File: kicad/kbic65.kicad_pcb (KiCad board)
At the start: 2 copper layers, 313.3 x 131.6 mm, 154 parts, among them U1 ProMicro

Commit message: pre-updating gnd
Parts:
- added ?: , , B.Cu at (-0.79, 166.7)
- added ?: , , B.Cu at (56.4, 83.3)
- R Shift: renamed from RShift
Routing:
- net Net-(D_Equal1-Pad2): track 35.2 -> 31.6 mm
- net Net-(D_@1-Pad2): track 79.2 -> 76.4 mm
- net Net-(D_LBKT1-Pad2): track 53.1 -> 50.6 mm
- net Net-(D_BKSLSH1-Pad2): track 93.8 -> 94.4 mm
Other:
- board text added: "#"
- board text added: "'"
- board text added: ","
- board text added: "-"
- board text added: "."
- board text added: "/"
- board text added: "0"
- board text added: "1"
- board text added: "1.25u"
- board text added: "1u"
- board text added: "2"
- board text added: "2.25u"
- board text added: "2u"
- board text added: "3"
- board text added: "4"
- board text added: "5"
- board text added: "6"
- board text added: "6.25u"
- board text added: "6u"
- board text added: "7"
- board text added: "8"
- board text added: "9"
- board text added: ";"
- board text added: "="
- board text added: "A"
- board text added: "B"
- board text added: "Backspace"
- board text added: "Backspace 2"
- board text added: "C"
- board text added: "Caps Lock"
- board text added: "D"
- board text added: "Delete"
- board text added: "Down"
- board text added: "E"
- board text added: "Enter"
- board text added: "Enter ANSI"
- board text added: "Esc"
- board text added: "F"
- board text added: "G"
- board text added: "H"
- board text added: "I"
- board text added: "J"
- board text added: "K"
- board text added: "L"
- board text added: "L Alt"
- board text added: "L Ctrl"
- board text added: "L Shift"
- board text added: "L Win"
- board text added: "Left"
- board text added: "M"
- board text added: "N"
- board text added: "O"
- board text added: "P"
- board text added: "Page Down"
- board text added: "Page Up"
- board text added: "Q"
- board text added: "R"
- board text added: "R Alt"
- board text added: "R Ctrl"
- board text added: "R Shift"
- board text added: "R Win"
- board text added: "Regular"
- board text added: "Right"
- board text added: "S"
- board text added: "Space"
- board text added: "Stepped"
- board text added: "T"
- board text added: "Tab"
- board text added: "U"
- board text added: "Up"
- board text added: "V"
- board text added: "W"
- board text added: "X"
- board text added: "Y"
- board text added: "Z"
- board text added: "["
- board text added: "\"
- board text added: "\ ANSI"
- board text added: "]"
- board text added: "¬"

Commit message: adding copper fill
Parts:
- MX_BkSlsh1: renamed from \ ANSI
- MX_BkSp2: renamed from Backpace 2
- MX_BkSp3_2u1: renamed from BkSp 3
- MX_CpsLck1: renamed from Caps Lock
- MX_Enter1: renamed from Enter ANSI
- MX_LAlt1: renamed from L Alt
- MX_LCtrl1: renamed from L Ctrl
- MX_LShift_ISO1: renamed from L Shift
- MX_LWin1: renamed from L Win
- MX_PgDn1: renamed from Page Down
- MX_PgUp1: renamed from Page Up
- MX_RAlt3_1.25u_6.25u_space1: renamed from R Alt
- MX_RCtrl1: renamed from R Ctrl
- MX_RShift1: renamed from R Shift
- MX_RWin1: renamed from R Win
- renumbered 0 to D_0, 1 to D_1, 2 to D_2, 3 to D_3, 4 to D_4, 5 to D_5, 6 to D_6, 7 to D_7, 8 to D_8, 9 to D_9, ' to D_@1, A to D_A1, B to D_B1, \ to D_BKSLSH1, BkSp to D_BkSp1, BkSp2 to D_BkSp2, C to D_C1, , to D_Comma1, CpsLck to D_CpsLck1, D to D_D1, Del to D_Del1, . to D_Dot1, Down to D_Down1, E to D_E1, # to D_Enter1, = to D_Equal1, Esc to D_Esc1, F to D_F1, / to D_FwdSlsh1, G to D_G1, H to D_H1, - to D_Hyphen1, I to D_I1, \ to D_ISO_BKSLSH1, J to D_J1, K to D_K1, L to D_L1, LAlt to D_LAlt1, [ to D_LBKT1, LCtrl to D_LCtrl1, LShift to D_LShift1, LWin to D_LWin1, Left to D_Left1, M to D_M1, N to D_N1, O to D_O1, P to D_P1, PgDn to D_PgDn1, PgUp to D_PgUp1, Q to D_Q1, R to D_R1, RAlt to D_RAlt1, ] to D_RBKT1, RCtrl to D_RCtrl1, RShift to D_RShift1, RWin to D_RWin1, Right to D_Right1, S to D_S1, ; to D_SemiCol1, Space to D_Space1, T to D_T1, Tab to D_Tab1, ¬ to D_Tilde1, U to D_U1, Up to D_Up1, V to D_V1, W to D_W1, X to D_X1, Y to D_Y1, Z to D_Z1, 0 to MX_0, 1 to MX_1, 2 to MX_2, 3 to MX_3, 4 to MX_4, 5 to MX_5, 6 to MX_6, 7 to MX_7, 8 to MX_8, 9 to MX_9, ' to MX_@1, A to MX_A1, B to MX_B1, Enter to MX_BkSlash2_ISO_Enter1, Backspace to MX_BkSp1, C to MX_C1, , to MX_Comma1, D to MX_D1, Delete to MX_Del1, . to MX_Dot1, Down to MX_Down1, E to MX_E1, # to MX_Enter2_ISO_Hash1, = to MX_Equal1, Esc to MX_Esc1, F to MX_F1, / to MX_FwdSlsh1, G to MX_G1, H to MX_H1, - to MX_Hyphen1, I to MX_I1, \ to MX_ISO_BKSLSH1, J to MX_J1, K to MX_K1, L to MX_L1, [ to MX_LBKT1, Left to MX_Left1, M to MX_M1, N to MX_N1, O to MX_O1, P to MX_P1, Q to MX_Q1, R to MX_R1, ] to MX_RBKT1, Right to MX_Right1, S to MX_S1, ; to MX_SemiCol1, Space to MX_Space1_6.25u1, T to MX_T1, Tab to MX_Tab1, ¬ to MX_Tilde1, U to MX_U1, Up to MX_Up1, V to MX_V1, W to MX_W1, X to MX_X1, Y to MX_Y1, Z to MX_Z1
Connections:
- U1 pad 23: Net-(U1-Pad23) -> GND
- U1 pad 3: Net-(U1-Pad3) -> GND
- U1 pad 4: Net-(U1-Pad4) -> GND
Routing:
- net Net-(D_ISO_BKSLSH1-Pad2): track 104.4 -> 105.8 mm
- net COL2: track 106.6 -> 107.3 mm
- added copper zone on B.Cu, net GND
- added copper zone on F.Cu, net GND

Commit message: readded missing silkscreen text
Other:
- board text added: "BkSp1"
- board text added: "BkSp2"
- board text added: "CpsLck"
- board text added: "Del"
- board text added: "LAlt"
- board text added: "LCtrl"
- board text added: "LShift"
- board text added: "LWin"
- board text added: "PgDn"
- board text added: "PgUp"
- board text added: "RAlt"
- board text added: "RCtrl"
- board text added: "RShift"
- board text added: "RWin"

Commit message: added signature
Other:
- board text added: "by KarlB"
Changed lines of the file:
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@@
   (general
     (thickness 1.6)
-    (drawings 1227)
+    (drawings 1229)
     (tracks 968)
     (zones 0)
@@
   (page A3)
   (layers
-    (0 F.Cu signal hide)
-    (31 B.Cu signal hide)
+    (0 F.Cu signal)
+    (31 B.Cu signal)
     (32 B.Adhes user)
     (33 F.Adhes user)
     (34 B.Paste user)
     (35 F.Paste user)
-    (36 B.SilkS user)
+    (36 B.SilkS user hide)
     (37 F.SilkS user)
     (38 B.Mask user)
@@
     )
   )
+  (gr_text "by KarlB" (at 59.5 50) (layer B.SilkS)
+    (effects (font (size 2 2) (thickness 0.2) italic) (justify mirror))
+  )
+  (gr_text "by KarlB" (at 64.75 53.75) (layer F.SilkS)
+    (effects (font (size 2 2) (thickness 0.2) italic))
+  )
   (gr_text 1 (at 87.75 56.128095) (layer B.SilkS)

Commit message: added styled lines to top
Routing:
- net GND: track 0.00 -> 1478.9 mm, vias 0 -> 1

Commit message: added ref placeholders and created gerbers
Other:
- board text added: "JLCJLCJLCJLC"
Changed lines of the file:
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@@
   (general
     (thickness 1.6)
-    (drawings 1235)
+    (drawings 1237)
     (tracks 988)
     (zones 0)
@@
   (page A3)
   (layers
-    (0 F.Cu signal)
-    (31 B.Cu signal)
+    (0 F.Cu signal hide)
+    (31 B.Cu signal hide)
     (32 B.Adhes user)
     (33 F.Adhes user)
@@
     (visible_elements 7FFDFFFF)
     (pcbplotparams
-      (layerselection 0x010fc_ffffffff)
+      (layerselection 0x013f0_ffffffff)
       (usegerberextensions false)
       (usegerberattributes true)
@@
       (outputformat 1)
       (mirror false)
-      (drillshape 1)
+      (drillshape 0)
       (scaleselection 1)
-      (outputdirectory ""))
+      (outputdirectory "gerber"))
   )
   (net 0 "")
@@
     )
   )
+  (gr_poly (pts (xy 328.824999 44.55) (xy 327.504999 44.7) (xy 326.344999 44.92) (xy 325.244999 45.3) (xy 324.794999 45.45) (xy 325.024999 47.38) (xy 326.614999 47.24) (xy 326.654999 46.36) (xy 327.004999 45.88) (xy 327.144999 45.73) (xy 327.614999 45.56) (xy 328.014999 45.44) (xy 329.424999 45.29) (xy 331.464999 45.21) (xy 332.674999 45.19) (xy 335.514999 45.39) (xy 337.184999 45.59) (xy 337.664999 45.7) (xy 338.154999 45.91) (xy 338.514999 46.16) (xy 338.804999 46.42) (xy 338.954999 46.71) (xy 339.064999 47.04) (xy 339.124999 47.5) (xy 339.174999 47.83) (xy 339.794999 47.81) (xy 339.844999 47.05) (xy 339.784999 46.5) (xy 339.384999 45.85) (xy 338.734999 45.43) (xy 338.174999 45.17) (xy 337.144999 44.92) (xy 334.714999 44.58) (xy 333.094999 44.54) (xy 330.304999 44.49)) (layer F.SilkS) (width 0.1))
+  (gr_text JLCJLCJLCJLC (at 73.025 98.425 90) (layer F.SilkS)
+    (effects (font (size 1 1) (thickness 0.15)))
+  )
   (gr_line (start 319 56.75) (end 86.5 56.75) (layer F.Mask) (width 0.25))
   (gr_line (start 319 55.75) (end 86.5 55.75) (layer F.Mask) (width 0.25))
@@
     (effects (font (size 1 1) (thickness 0.15)))
   )
-  (gr_poly (pts (xy 353.8 44.55) (xy 355.12 44.7) (xy 356.28 44.92) (xy 357.38 45.3) (xy 357.83 45.45) (xy 357.6 47.38) (xy 356.01 47.24) (xy 355.97 46.36) (xy 355.62 45.88) (xy 355.48 45.73) (xy 355.01 45.56) (xy 354.61 45.44) (xy 353.2 45.29) (xy 351.16 45.21) (xy 349.95 45.19) (xy 347.11 45.39) (xy 345.44 45.59) (xy 344.96 45.7) (xy 344.47 45.91) (xy 344.11 46.16) (xy 343.82 46.42) (xy 343.67 46.71) (xy 343.56 47.04) (xy 343.5 47.5) (xy 343.45 47.83) (xy 342.83 47.81) (xy 342.78 47.05) (xy 342.84 46.5) (xy 343.24 45.85) (xy 343.89 45.43) (xy 344.45 45.17) (xy 345.48 44.92) (xy 347.91 44.58) (xy 349.53 44.54) (xy 352.32 44.49)) (layer F.SilkS) (width 0.1))
+  (gr_poly (pts (xy 353.8 44.55) (xy 355.12 44.7) (xy 356.28 44.92) (xy 357.38 45.3) (xy 357.812961 45.475356) (xy 357.593378 47.440046) (xy 356.019031 47.225625) (xy 355.97 46.36) (xy 355.62 45.88) (xy 355.48 45.73) (xy 355.01 45.56) (xy 354.61 45.44) (xy 353.2 45.29) (xy 351.16 45.21) (xy 349.95 45.19) (xy 347.11 45.39) (xy 345.44 45.59) (xy 344.96 45.7) (xy 344.47 45.91) (xy 344.11 46.16) (xy 343.82 46.42) (xy 343.67 46.71) (xy 343.56 47.04) (xy 343.5 47.5) (xy 343.443634 47.844032) (xy 342.857268 47.823973) (xy 342.78 47.05) (xy 342.84 46.5) (xy 343.24 45.85) (xy 343.89 45.43) (xy 344.45 45.17) (xy 345.48 44.92) (xy 347.91 44.58) (xy 349.53 44.54) (xy 352.32 44.49)) (layer F.SilkS) (width 0.1))
   (gr_line (start 49.085386 165.775001) (end 49.085386 165.775001) (layer Edge.Cuts) (width 0.2))
   (gr_line (start 46.585405 163.275001) (end 46.585399 42.30625) (layer Edge.Cuts) (width 0.2))
@@
   (gr_line (start 62.562499 72.374992) (end 62.562499 86.375408) (layer Dwgs.User) (width 0.2))
   (gr_line (start 48.562083 72.374992) (end 62.562499 72.374992) (layer Dwgs.User) (width 0.2))
-  (via (at 320 50) (size 0.8) (drill 0.4) (layers F.Cu B.Cu) (net 92))
-  (segment (start 86.5 43.25) (end 319 43.25) (width 0.3) (layer F.Cu) (net 92))
-  (segment (start 86.5 43.75) (end 319 43.75) (width 0.3) (layer F.Cu) (net 92))
-  (segment (start 86.5 44.25) (end 319 44.25) (width 0.3) (layer F.Cu) (net 92))
-  (segment (start 86.5 56.25) (end 319 56.25) (width 0.3) (layer F.Cu) (net 92))
-  (segment (start 86.5 55.75) (end 319 55.75) (width 0.3) (layer F.Cu) (net 92))
-  (segment (start 86.5 56.75) (end 319 56.75) (width 0.3) (layer F.Cu) (net 92))
   (segment (start 238.83506 76.835) (end 237.25006 75.25) (width 0.25) (layer B.Cu) (net 1))
   (segment (start 242.2525 76.835) (end 238.83506 76.835) (width 0.25) (layer B.Cu) (net 1) (status 10))
@@
   (segment (start 62.07125 48.82125) (end 62.07125 42.15765) (width 0.25) (layer F.Cu) (net 87) (status 20))
   (segment (start 63.75001 50.50001) (end 62.07125 48.82125) (width 0.25) (layer F.Cu) (net 87))
+  (via (at 320 50) (size 0.8) (drill 0.4) (layers F.Cu B.Cu) (net 92))
+  (segment (start 86.5 43.25) (end 319 43.25) (width 0.3) (layer F.Cu) (net 92))
+  (segment (start 86.5 43.75) (end 319 43.75) (width 0.3) (layer F.Cu) (net 92))
+  (segment (start 86.5 44.25) (end 319 44.25) (width 0.3) (layer F.Cu) (net 92))
+  (segment (start 86.5 56.25) (end 319 56.25) (width 0.3) (layer F.Cu) (net 92))
+  (segment (start 86.5 55.75) (end 319 55.75) (width 0.3) (layer F.Cu) (net 92))
+  (segment (start 86.5 56.75) (end 319 56.75) (width 0.3) (layer F.Cu) (net 92))
   (segment (start 56.99125 57.85485) (end 56.99125 68.74125) (width 0.25) (layer F.Cu) (net 92))
   (segment (start 57.44845 57.39765) (end 56.99125 57.85485) (width 0.25) (layer B.Cu) (net 92))
@@
   (zone (net 0) (net_name "") (layer F.SilkS) (hatch edge 0.508)
     (connect_pads (clearance 0.508))
-    (min_thickness 0.254)
-    (fill yes (arc_segments 32) (thermal_gap 0.508) (thermal_bridge_width 0.508))
-    (polygon
-      (pts
-        (xy 332.85 44.53) (xy 334.67 44.6) (xy 336.31 44.76) (xy 337.32 44.95) (xy 338.41 45.26)
-        (xy 339.27 45.77) (xy 339.69 46.28) (xy 339.86 46.92) (xy 339.76 47.81) (xy 339.17 47.8)
-        (xy 338.98 46.79) (xy 338.87 46.52) (xy 338.55 46.18) (xy 338.19 45.94) (xy 337.75 45.75)
-        (xy 336.78 45.54) (xy 335.06 45.35) (xy 333.64 45.23) (xy 332.21 45.17) (xy 330.95 45.21)
-        (xy 329.58 45.26) (xy 328.39 45.38) (xy 327.33 45.62) (xy 326.84 45.98) (xy 326.65 46.37)
-        (xy 326.56 46.83) (xy 326.57 47.24) (xy 325.06 47.43) (xy 324.84 45.44) (xy 326.48 44.89)
-        (xy 327.86 44.69) (xy 329.23 44.54) (xy 330.76 44.5)
-      )
-    )
-  )
-  (zone (net 0) (net_name "") (layer F.SilkS) (hatch edge 0.508)
-    (connect_pads (clearance 0.508))

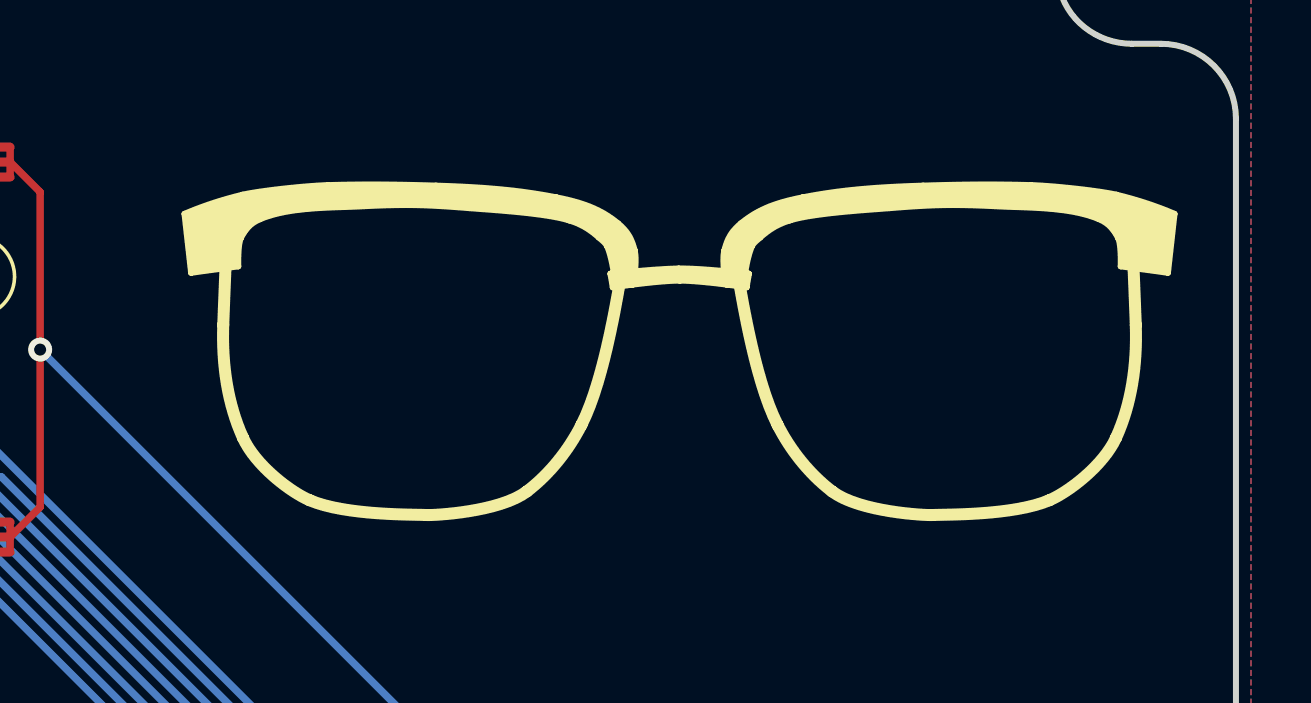
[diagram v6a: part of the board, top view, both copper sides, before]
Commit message: changed bottom glasses to cu
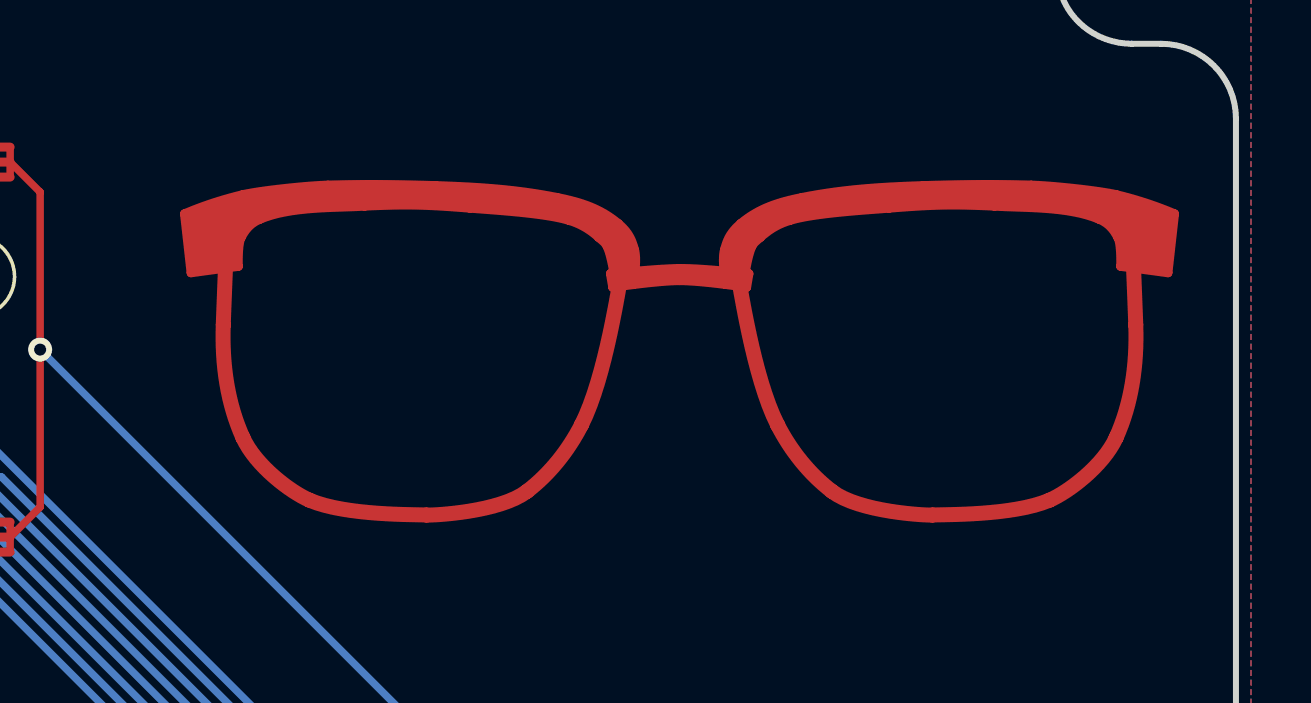
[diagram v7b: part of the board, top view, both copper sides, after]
